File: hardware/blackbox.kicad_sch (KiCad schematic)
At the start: 3 parts

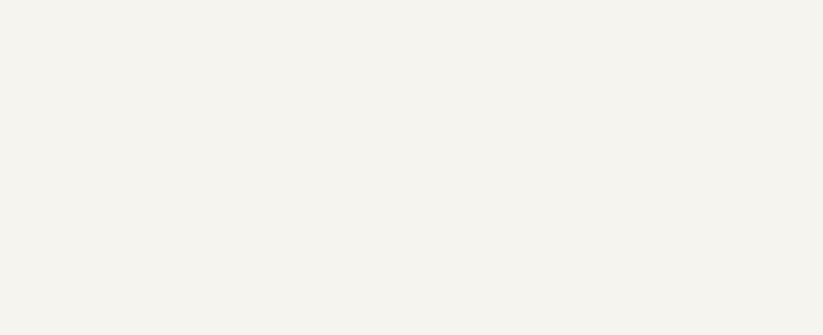
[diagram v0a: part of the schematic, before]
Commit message: docs(schematic): add design annotations to all sheets
Port on-canvas engineering comments from OpenFC-Lite (RP2354B), adapted to the
Mini layout. +41 text items across root, rp2350a, power, imu, osd, blackbox,
pads. Annotation/text only — no net or connectivity changes. Mirrors
hardware/DESIGN_NOTES.md.

Co-Authored-By: Claude Opus 4.8 (1M context) <noreply@anthropic.com>
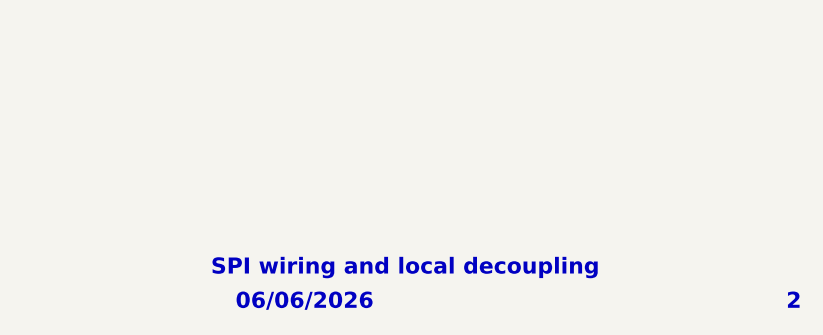
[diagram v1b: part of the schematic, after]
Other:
- note added: "06/06/2026"
- note added: "2"
- note added: "SPI wiring and local decoupling"
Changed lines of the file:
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@@
 		(title "BLACKBOX")
+	)
+	(text "2"
+		(exclude_from_sim no)
+		(at 182.88 131.318 0)
+		(effects
+			(font
+				(size 1.778 1.778)
+				(thickness 0.3556)
+				(bold yes)
+				(color 0 0 0 1)
+			)
+		)
+	)
+	(text "SPI wiring and local decoupling"
+		(exclude_from_sim no)
+		(at 139.7 127.508 0)
+		(effects
+			(font
+				(size 1.778 1.778)
+				(thickness 0.3556)
+				(bold yes)
+				(color 0 0 0 1)
+			)
+		)
+	)
+	(text "06/06/2026"
+		(exclude_from_sim no)
+		(at 128.524 131.318 0)
+		(effects
+			(font
+				(size 1.778 1.778)
+				(thickness 0.3556)
+				(bold yes)
+				(color 0 0 0 1)
+			)
+		)
 	)
 	(junction

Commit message: schematics: complete Manufacturer/MPN coverage, trim stray whitespace
22 field fixes across blackbox, osd, power, rp2350a: Manufacturer backfilled
from the LCSC catalogue, trailing space trimmed from four XL-1005UGC MPNs.
pads.kicad_sch (uncommitted WIP) untouched. Part of the fab-agnostic BOM
standardisation for quoting outside JLCPCB.

kicad-skip reflowed the touched files; structural diff shows only property
changes, ERC identical (163 violations before and after).

Co-Authored-By: Claude Fable 5 <noreply@anthropic.com>
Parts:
- Card1: MPN (none) -> TF-021B-H265; Manufacturer (none) -> SOFNG
